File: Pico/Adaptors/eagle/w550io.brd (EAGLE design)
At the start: 28.6 x 27.3 mm, 4 parts

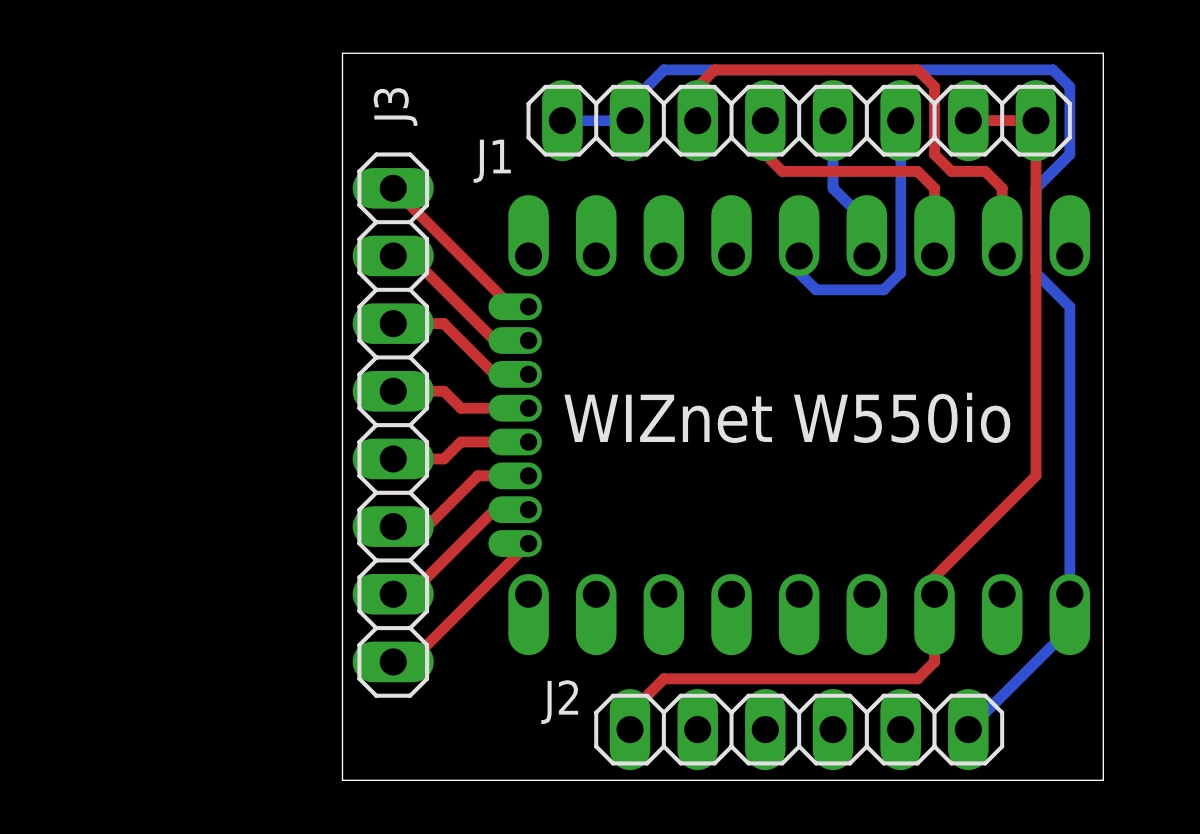
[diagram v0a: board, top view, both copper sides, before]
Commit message: oops - fix wiznet board
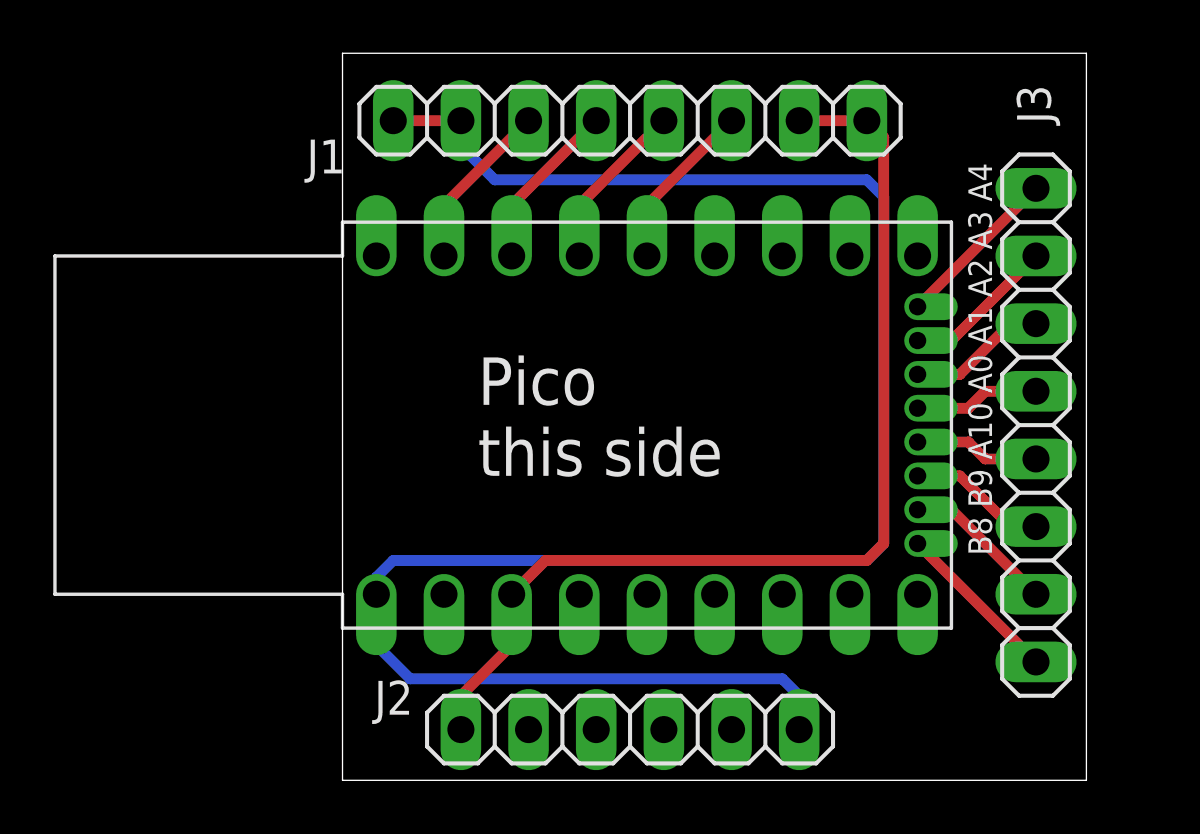
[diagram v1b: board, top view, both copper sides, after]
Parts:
- moved J3 24.1 mm to (26.0, 13.3)
- moved J1 6.35 mm to (10.8, 24.8)
- moved J2 6.35 mm to (10.8, 1.91)
- moved U$1 1.90 mm to (15.2, 13.3), flipped to the top
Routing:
- net GND: track 47.2 -> 73.2 mm
- net MOSI: track 18.8 -> 6.40 mm
- net MISO: track 10.7 -> 6.40 mm
- net SCS: track 10.7 -> 6.40 mm
- net 3V3: track 37.3 -> 39.3 mm
- net SCLK: track 5.61 -> 6.40 mm
- net N$2: track 6.40 -> 5.76 mm
- net N$8: track 6.92 -> 6.29 mm
- net N$7: track 6.40 -> 5.76 mm
- net N$6: track 5.87 -> 5.23 mm
- net N$3: track 5.87 -> 5.23 mm
- net N$1: track 6.92 -> 6.29 mm
- net N$5: track 5.34 -> 4.71 mm
- net N$4: track 5.34 -> 4.71 mm
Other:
- board size 28.6 x 27.3 mm -> 27.9 x 27.3 mm
- board text added: "Pico this side"
- board text removed: "Espruino Pio"

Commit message: more tweaks and options
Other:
- board size 27.9 x 27.3 mm -> 28.1 x 26.8 mm
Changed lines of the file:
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@@
 <setting verticaltext="up"/>
 </settings>
-<grid distance="0.05" unitdist="inch" unit="inch" style="lines" multiple="1" display="no" altdistance="0.0125" altunitdist="inch" altunit="inch"/>
+<grid distance="0.05" unitdist="inch" unit="inch" style="lines" multiple="1" display="no" altdistance="0.005" altunitdist="inch" altunit="inch"/>
 <layers>
 <layer number="1" name="Top" color="4" fill="1" visible="yes" active="yes"/>
@@
 <board>
 <plain>
-<wire x1="0" y1="0" x2="27.9275" y2="0" width="0" layer="20"/>
-<wire x1="27.9275" y1="0" x2="27.9275" y2="27.295" width="0" layer="20"/>
-<wire x1="27.9275" y1="27.295" x2="0" y2="27.295" width="0" layer="20"/>
-<wire x1="0" y1="27.295" x2="0" y2="0" width="0" layer="20"/>
+<wire x1="0" y1="0" x2="28.0545" y2="0" width="0" layer="20"/>
+<wire x1="28.0545" y1="0" x2="28.0545" y2="26.787" width="0" layer="20"/>
+<wire x1="28.0545" y1="26.787" x2="0" y2="26.787" width="0" layer="20"/>
+<wire x1="0" y1="26.787" x2="0" y2="0" width="0" layer="20"/>
 <text x="20.0025" y="16.51" size="1.778" layer="22" rot="MR0">WIZnet W550io</text>
 <text x="23.495" y="23.1775" size="0.889" layer="21" rot="R270">B8 B9 A10 A0 A1 A2 A3 A4</text>
@@
 <element name="U$1" library="espruino_pico" package="ESPRUINO_PICO_SMD" value="ESPRUINO_PICO_SMD" x="15.24" y="13.335"/>
 <element name="J1" library="pinhead" package="1X08" value="" x="10.795" y="24.765" smashed="yes">
-<attribute name="NAME" x="-1.3462" y="22.7838" size="1.27" layer="25" ratio="10"/>
+<attribute name="NAME" x="21.5138" y="25.3238" size="1.27" layer="25" ratio="10"/>
 <attribute name="VALUE" x="0.635" y="21.59" size="1.27" layer="27"/>
 </element>
 <element name="J2" library="pinhead" package="1X06" value="" x="10.795" y="1.905" smashed="yes">
-<attribute name="NAME" x="1.1938" y="2.4638" size="1.27" layer="25" ratio="10"/>
+<attribute name="NAME" x="18.9738" y="2.4638" size="1.27" layer="25" ratio="10"/>
 <attribute name="VALUE" x="3.175" y="-1.27" size="1.27" layer="27"/>
 </element>
 <element name="J3" library="pinhead" package="1X08" value="" x="26.035" y="13.335" smashed="yes" rot="R270">
-<attribute name="NAME" x="25.3238" y="26.1112" size="1.27" layer="25" ratio="10" rot="R270"/>
 <attribute name="VALUE" x="22.86" y="23.495" size="1.27" layer="27" rot="R270"/>
 </element>
